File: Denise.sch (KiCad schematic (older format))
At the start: 45 parts, among them CN450 VIDEO OUT, CN451 Video_Edge, U450 Denise, U451 74HCT244*, U452 74HCT244, U710 74F08

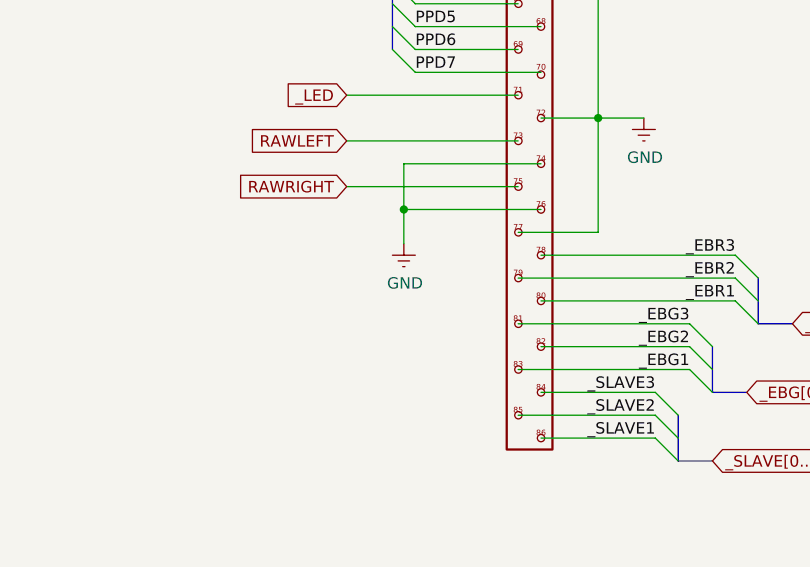
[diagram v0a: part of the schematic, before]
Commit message: Minor changes to schematics
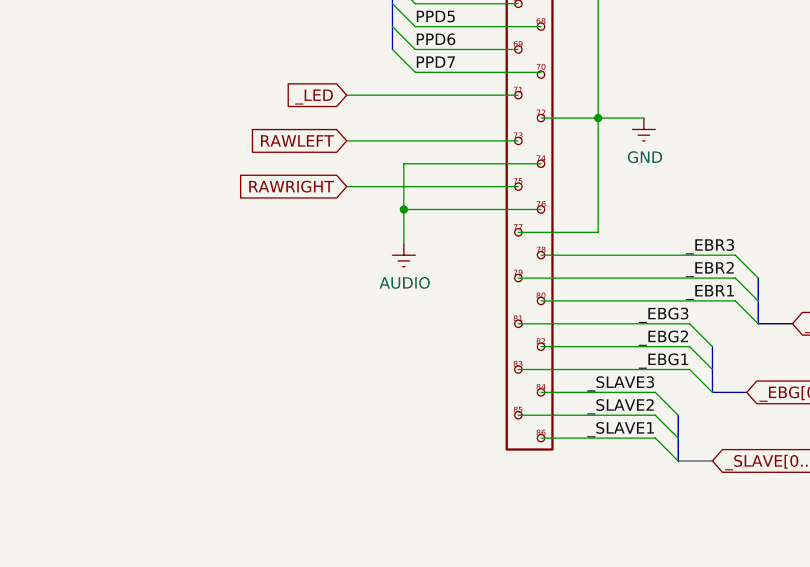
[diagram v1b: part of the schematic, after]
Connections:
- net GND: no longer CN451.74, CN451.76
- new net AUDIO: CN451.74, CN451.76
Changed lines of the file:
@@
 Wire Wire Line
 	12450 8400 13200 8400
-$Comp
-L Amiga_3000_library:GND #PWR0279
-U 1 1 6047F8D4
-P 12700 8650
-F 0 "#PWR0279" H 12700 8400 50  0001 C CNN
-F 1 "GND" H 12705 8477 50  0000 C CNN
-F 2 "" H 12700 8650 50  0001 C CNN
-F 3 "" H 12700 8650 50  0001 C CNN
-	1    12700 8650
-	1    0    0    -1
-$EndComp
 Wire Wire Line
 	13300 8300 12700 8300
@@
 Wire Bus Line
 	3400 1900 3400 3450
+$Comp
+L Amiga_3000_library:AUDIO #PWR0168
+U 1 1 6087EF1A
+P 12700 8650
+F 0 "#PWR0168" H 12700 8400 50  0001 C CNN
+F 1 "AUDIO" H 12705 8477 50  0000 C CNN
+F 2 "" H 12700 8650 50  0001 C CNN
+F 3 "" H 12700 8650 50  0001 C CNN
+	1    12700 8650
+	1    0    0    -1
+$EndComp
 $EndSCHEMATC
